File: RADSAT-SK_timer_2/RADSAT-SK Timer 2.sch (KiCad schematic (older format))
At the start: 54 parts, among them J201 Conn_01x07, J202 Conn_01x05, J203 Conn_01x03, J204 Conn_01x02, J205 Conn_01x02, J206 Conn_01x02, Q201 IRLML2060, Q202 IRLML2060, Q204 IRLML2060, Q205 IRLML2060, Q206 IRLML2060, Q207 IRLML2060, SW201 SW_Push, SW202 SW_Push, SW203 SW_Push, SW204 SW_Push, SW205 SW_Push, SW206 SW_Push, U202 LTC3440EMSPBF, U230 CPC1114N, U240 CPC1114N, U250 CPC1114N, U260 CPC1114N

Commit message: changed RBF logic and added footprint for J202
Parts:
- removed C204: 10uF, Capacitor_SMD:C_0805_2012Metric, symbol Device:C
- removed C205: 0.1uF, Capacitor_SMD:C_0805_2012Metric, symbol Device:C
- removed C207: 1.5nF, Capacitor_SMD:C_0805_2012Metric, symbol Device:C
- removed C208: 22uF, Capacitor_SMD:C_1210_3225Metric_Pad1.33x2.70mm_HandSolder, symbol Device:C
- removed D201: 5.0SMDJ5.0A, Diode_SMD:D_SMC_Handsoldering, symbol Diode:SM6T6V8A
- removed D203: MBRM120LT3G, Diode_SMD:D_Powermite_AK, symbol Device:D_Schottky
- removed J202: Conn_01x05, Connector_Hirose:Hirose_DF13-05P-1.25DSA_1x05_P1.25mm_Vertical, symbol Connector_Generic:Conn_01x05
- removed L201: 10uH, Sumida_inductor:Sumida_inductor, symbol Device:L
- removed Q201, Q202, Q207: IRLML2060, Package_TO_SOT_SMD:SOT-23_Handsoldering, symbol Transistor_FET:IRLML2060
- removed R201: 3M, Resistor_SMD:R_0805_2012Metric, symbol Device:R
- removed R202, R204, R220: 100, Resistor_SMD:R_0805_2012Metric, symbol Device:R
- removed R203, R221: 1M, Resistor_SMD:R_0805_2012Metric, symbol Device:R
- removed R205: 60.4K, Resistor_SMD:R_0805_2012Metric, symbol Device:R
- removed R206: 15k, Resistor_SMD:R_0805_2012Metric, symbol Device:R
- removed R207: 619k, Resistor_SMD:R_0805_2012Metric, symbol Device:R
- removed R208: 200k, Resistor_SMD:R_0805_2012Metric, symbol Device:R
- removed U202: LTC3440EMSPBF, Package_SO:MSOP-10_3x3mm_P0.5mm, symbol LTC3440EMSPBF:LTC3440EMSPBF
- added H101, H102, H103, H104: MountingHole, MountingHole:MountingHole_3.2mm_M3_ISO7380_Pad_TopBottom, symbol Mechanical:MountingHole
- added J101, J103: Conn_02x26_Odd_Even, Connector_PinSocket_2.54mm:PinSocket_2x26_P2.54mm_Vertical, symbol Connector_Generic:Conn_02x26_Odd_Even
- added J202: Conn_01x04_Female, Connector_Hirose:Hirose_DF13-04P-1.25DSA_1x04_P1.25mm_Vertical, symbol Connector:Conn_01x04_Female
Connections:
- wire segments 154 -> 103
- no-connect marks 3 -> 95
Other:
- note added: "CSKB Connectors"
- note added: "Mechanical Switches and RBF Connection with 5vCharge"
- note added: "Mounting Holes\n"
- note added: "RBF IN: Short Pins 4, 2\nRBF OUT: Pins OPEN\nCHARGE PIN: PINS 1,3 OPEN, 5V Pin 1"
- note added: "Riley Nemetz\nAtharva Kulkarni"
- note removed: "Battery Boost, Mechanical Switches and RBF Connection with 5vCharge"
- note removed: "RBF IN: Short Pins 1, 2\nRBF OUT: Pins OPEN\nCHARGE PIN: PINS 1,2 OPEN, 5V Pin 3"
- note removed: "Riley Nemetz"
- moved on the sheet: D204A, D204B, D206, J203, R209, R210, U230

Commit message: new RBF logic and charging circuit!!
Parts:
- removed J202: Conn_01x04_Female, Connector_Hirose:Hirose_DF13-04P-1.25DSA_1x04_P1.25mm_Vertical, symbol Connector:Conn_01x04_Female
- added BT202: Battery_Cell, Battery:BatteryHolder_Keystone_1060_1x2032, symbol Device:Battery_Cell
- added C?: 2.2uF, Capacitor_SMD:C_0805_2012Metric, symbol Device:C
- added C?: 7pF, Capacitor_SMD:C_0805_2012Metric, symbol Device:C
- added C?: 1uF, Capacitor_SMD:C_0805_2012Metric, symbol Device:C
- added C?: 0.1uF, Capacitor_SMD:C_0805_2012Metric, symbol Device:C
- added D?: RB751V40T1G, Diode_SMD:D_SOD-323, symbol Device:D_Schottky
- added D?: LED, LED_SMD:LED_0805_2012Metric, symbol Device:LED
- added J202: Conn_01x05_Female, symbol Connector:Conn_01x05_Female
- added R?: 560, Resistor_SMD:R_0805_2012Metric, symbol Device:R
- added R?: 1k, Resistor_SMD:R_0805_2012Metric, symbol Device:R
- added R?: 51.1k, Resistor_SMD:R_0805_2012Metric, symbol Device:R
- added R?: 76.8k, Resistor_SMD:R_0805_2012Metric, symbol Device:R
- added R?: 10k, Resistor_SMD:R_0805_2012Metric, symbol Device:R
- added R?: 100k, Resistor_SMD:R_0805_2012Metric, symbol Device:R
- added R?: 49.9k, Resistor_SMD:R_0805_2012Metric, symbol Device:R
- added R?: 604K, Resistor_SMD:R_0805_2012Metric, symbol Device:R
- added U201: LP2980IM5-5.0, Package_TO_SOT_SMD:TSOT-23-5, symbol RADSAT-SK-Timer-rescue:LP2980IM5-5.0-LP2980IM5-5.0
- added U202: TPS3700DDCR, Package_TO_SOT_SMD:TSOT-23-6, symbol RADSAT-SK-Timer-rescue:TPS3700DDCR-TPS3700DDCR
- renumbered BT202 to BT203, J101 to J201, J103 to J203
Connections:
- net labels added: A, B, CHRG_ON-OFF
- wire segments 103 -> 158
- no-connect marks 95 -> 96
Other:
- note added: "Battery Charging\n"
- moved on the sheet: D204A, D204B, D?, J201, J203, R209, R210, U230

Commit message: annotated part numbers (generated netlist)
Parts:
- gave numbers to parts that had none: 14
- renumbered D206 to D101, D205 to D104, H103 to H102, H102 to H103, J201 to J207, J203 to J208, Q206 to Q101, Q204 to Q102, Q205 to Q103, R217 to R109

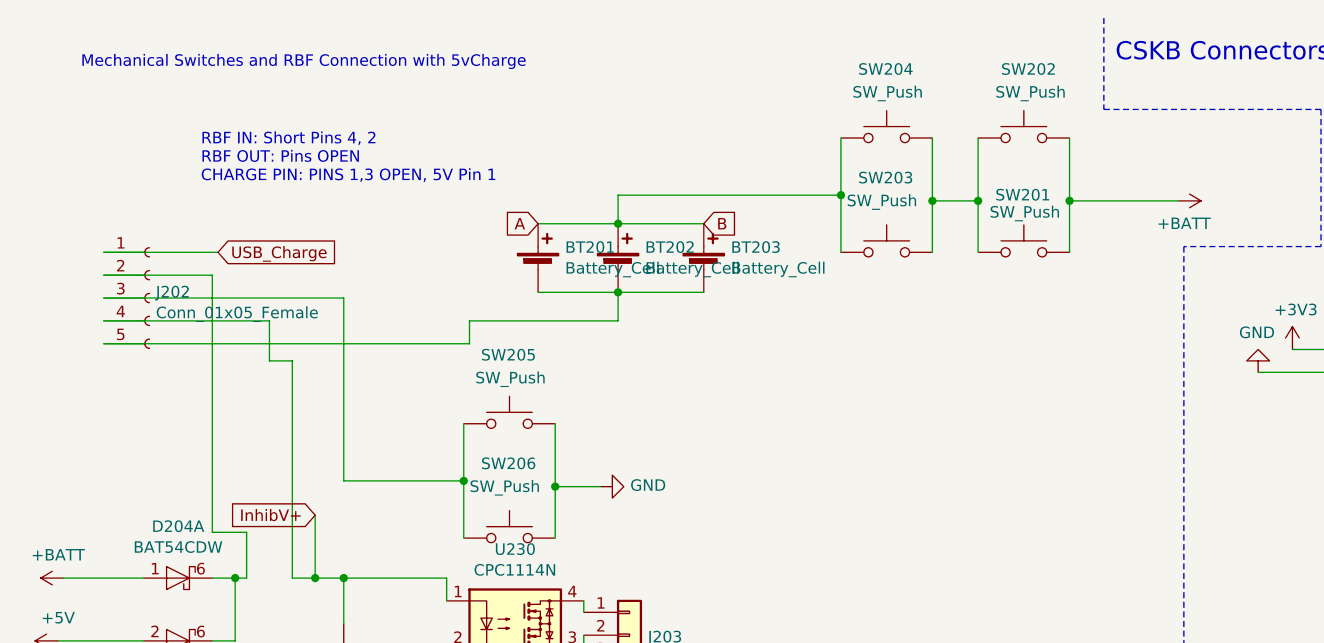
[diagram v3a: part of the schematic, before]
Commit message: switched out pin 3 and 5 on RBF pin
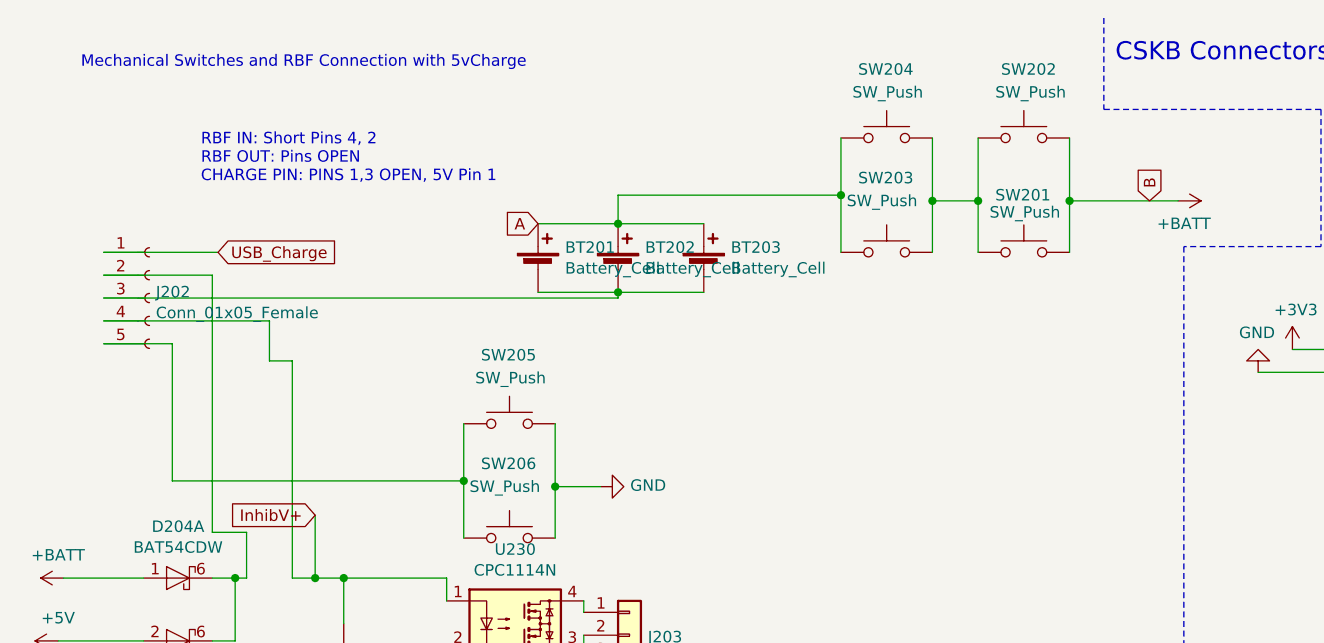
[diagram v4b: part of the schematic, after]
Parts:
- J202: footprint (none) -> Connector_Hirose:Hirose_DF13-05P-1.25DSA_1x05_P1.25mm_Vertical
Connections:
- wire segments 158 -> 156
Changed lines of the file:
@@
 Inhib_in
-$Comp
-L Device:Battery_Cell BT203
-U 1 1 600CC811
-P 3425 1575
-F 0 "BT203" H 3543 1671 50  0000 L CNN
-F 1 "Battery_Cell" H 3543 1580 50  0000 L CNN
-F 2 "Battery:BatteryHolder_Keystone_1060_1x2032" V 3425 1635 50  0001 C CNN
-F 3 "~" V 3425 1635 50  0001 C CNN
-	1    3425 1575
-	1    0    0    -1
-$EndComp
 $Comp
 L Device:Battery_Cell BT201
@@
 Wire Wire Line
 	2700 1675 3050 1675
-Wire Wire Line
-	3050 1800 3050 1675
 Connection ~ 3050 1675
 Wire Wire Line
@@
 Mounting Holes\n
 Wire Wire Line
-	2400 1900 2400 1800
-Wire Wire Line
-	2400 1800 3050 1800
-Wire Wire Line
-	800  1900 2400 1900
-Wire Wire Line
 	800  1800 1525 1800
 Wire Wire Line
@@
 Wire Wire Line
 	800  1500 1300 1500
-Wire Wire Line
-	800  1700 1850 1700
-Wire Wire Line
-	1850 1700 1850 2500
-Wire Wire Line
-	1850 2500 2375 2500
 $Comp
 L Connector:Conn_01x05_Female J202
@@
 F 0 "J202" H 1028 1726 50  0000 L CNN
 F 1 "Conn_01x05_Female" H 1028 1635 50  0000 L CNN
-F 2 "" H 1000 1700 50  0001 C CNN
+F 2 "Connector_Hirose:Hirose_DF13-05P-1.25DSA_1x05_P1.25mm_Vertical" H 1000 1700 50  0001 C CNN
 F 3 "~" H 1000 1700 50  0001 C CNN
 	1    1000 1700
@@
 Text GLabel 2700 1375 0    50   Input ~ 0
 A
-Text GLabel 3425 1375 2    50   Input ~ 0
-B
 Wire Wire Line
 	1625 2925 1725 2925
@@
 Text Notes 5375 5125 0    50   ~ 0
 Battery Charging\n
+$Comp
+L Device:Battery_Cell BT203
+U 1 1 600CC811
+P 3425 1575
+F 0 "BT203" H 3543 1671 50  0000 L CNN
+F 1 "Battery_Cell" H 3543 1580 50  0000 L CNN
+F 2 "Battery:BatteryHolder_Keystone_1060_1x2032" V 3425 1635 50  0001 C CNN
+F 3 "~" V 3425 1635 50  0001 C CNN
+	1    3425 1575
+	1    0    0    -1
+$EndComp
+Text GLabel 5375 1275 1    50   Input ~ 0
+B
+Wire Wire Line
+	1100 2500 1100 1900
+Wire Wire Line
+	1100 1900 800  1900
+Wire Wire Line
+	1100 2500 2375 2500
+Wire Wire Line
+	3050 1675 3050 1700
+Wire Wire Line
+	800  1700 3050 1700
 $EndSCHEMATC

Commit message: fixed RBF logic (back to initial state) and added test points
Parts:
- removed D101, D104: LED, LED_SMD:LED_0603_1608Metric_Pad1.05x0.95mm_HandSolder, symbol Device:LED
- removed R109, R209: 1k, Resistor_SMD:R_0805_2012Metric, symbol Device:R
- added J209: Conn_01x15, symbol Connector_Generic:Conn_01x15
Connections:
- net labels added: Test_CHRG_ON-OFF, Test_CSKB_3V3, Test_CSKB_5V, Test_GND, Test_I2C_CLK, Test_I2C_DATA, Test_INA+, Test_INB-, Test_InhibV+, Test_Relay_Inhibs, Test_SW1, Test_SW2, Test_USB_Charge, Test_Vreg, Test_negetive_Batt
- wire segments 156 -> 184

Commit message: deleted extra LEDs
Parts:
- removed D103: LED, LED_SMD:LED_0805_2012Metric, symbol Device:LED
- removed R106: 1k, Resistor_SMD:R_0805_2012Metric, symbol Device:R
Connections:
- wire segments 184 -> 180
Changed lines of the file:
@@
 Wire Wire Line
 	5450 4375 5525 4375
-Connection ~ 4975 4375
 $Comp
 L Device:D_Schottky D?
@@
 Wire Wire Line
 	4000 4700 3575 4700
-Connection ~ 4500 5050
-Wire Wire Line
-	4975 5050 4500 5050
-Wire Wire Line
-	4975 5025 4975 5050
 Connection ~ 4500 4375
-Wire Wire Line
-	4500 4375 4975 4375
-Wire Wire Line
-	4975 4675 4975 4725
-$Comp
-L Device:LED D?
-U 1 1 62C79500
-P 4975 4525
-AR Path="/62B9869E/62C79500" Ref="D?"  Part="1"
-AR Path="/62C79500" Ref="D103"  Part="1"
-F 0 "D103" V 5014 4407 50  0000 R CNN
-F 1 "LED" V 4923 4407 50  0000 R CNN
-F 2 "LED_SMD:LED_0805_2012Metric" H 4975 4525 50  0001 C CNN
-F 3 "~" H 4975 4525 50  0001 C CNN
-	1    4975 4525
-	0    -1   -1   0
-$EndComp
 Wire Wire Line
 	4000 5050 4275 5050
@@
 	1    5675 4375
 	0    -1   -1   0
-$EndComp
-$Comp
-L Device:R R?
-U 1 1 62C79529
-P 4975 4875
-AR Path="/62B9869E/62C79529" Ref="R?"  Part="1"
-AR Path="/62C79529" Ref="R106"  Part="1"
-F 0 "R106" H 5045 4921 50  0000 L CNN
-F 1 "1k" H 5045 4830 50  0000 L CNN
-F 2 "Resistor_SMD:R_0805_2012Metric" V 4905 4875 50  0001 C CNN
-F 3 "~" H 4975 4875 50  0001 C CNN
-	1    4975 4875
-	1    0    0    -1
 $EndComp
 $Comp
@@
 Wire Wire Line
 	5025 4150 5050 4150
-Wire Wire Line
-	4975 4375 5025 4375
 Connection ~ 5025 4375
 Wire Wire Line
@@
 Wire Wire Line
 	9025 4600 9200 4600
+Wire Wire Line
+	4500 4375 5025 4375
 $EndSCHEMATC

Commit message: added pull down resistors on relays
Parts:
- added R106, R109: 1M, symbol Device:R
- J209: footprint (none) -> Connector_Hirose:Hirose_DF13-15P-1.25DSA_1x15_P1.25mm_Vertical
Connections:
- wire segments 180 -> 185
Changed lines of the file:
@@
 	3100 6675 3100 7550
 Connection ~ 4475 7550
-Wire Wire Line
-	3100 6675 3025 6675
 Connection ~ 3100 6675
 Connection ~ 2925 6675
@@
 	2375 2525 2375 2750
 Wire Wire Line
-	2025 2925 2025 3275
-Wire Wire Line
-	1725 2925 2025 2925
+	2025 2925 2025 3525
+Wire Wire Line
+	1725 2925 1850 2925
 Connection ~ 2025 2925
 Wire Wire Line
@@
 Wire Notes Line
 	7950 5425 11225 5425
-Wire Wire Line
-	3025 6675 3025 7225
-Connection ~ 3025 6675
-Wire Wire Line
-	3025 6675 2925 6675
 Wire Wire Line
 	4525 1275 4525 850
@@
 F 0 "J209" V 10900 4525 50  0000 L CNN
 F 1 "Conn_01x15" V 10975 4400 50  0000 L CNN
-F 2 "" H 10800 4450 50  0001 C CNN
+F 2 "Connector_Hirose:Hirose_DF13-15P-1.25DSA_1x15_P1.25mm_Vertical" H 10800 4450 50  0001 C CNN
 F 3 "~" H 10800 4450 50  0001 C CNN
 	1    10800 4450
@@
 Text GLabel 10600 4050 0    50   Input ~ 0
 Test_SW2
-Text GLabel 2025 3275 3    50   Input ~ 0
+Text GLabel 2025 3525 3    50   Input ~ 0
 Test_InhibV+
 Text GLabel 10600 4150 0    50   Input ~ 0
@@
 Text GLabel 10600 4850 0    50   Input ~ 0
 Test_INB-
-Text GLabel 3025 7225 0    50   Input ~ 0
-Test_Relay_Inhibs
 Text GLabel 10600 4950 0    50   Input ~ 0
 Test_Relay_Inhibs
@@
 Wire Wire Line
 	4500 4375 5025 4375
+$Comp
+L Device:R R106
+U 1 1 62B16433
+P 2975 6950
+F 0 "R106" V 2875 6850 50  0000 L CNN
+F 1 "1M" V 2800 6900 50  0000 L CNN
+F 2 "" V 2905 6950 50  0001 C CNN
+F 3 "~" H 2975 6950 50  0001 C CNN
+	1    2975 6950
+	1    0    0    -1
+$EndComp
+$Comp
+L power:GND #PWR0122
+U 1 1 62B33151
+P 2975 7100
+F 0 "#PWR0122" H 2975 6850 50  0001 C CNN
+F 1 "GND" H 2875 7000 50  0000 C CNN
+F 2 "" H 2975 7100 50  0001 C CNN
+F 3 "" H 2975 7100 50  0001 C CNN
+	1    2975 7100
+	1    0    0    -1
+$EndComp
+Wire Wire Line
+	2975 6675 2975 6800
+Connection ~ 2975 6675
+Wire Wire Line
+	2975 6675 2925 6675
+Text GLabel 3000 7425 0    50   Input ~ 0
+Test_Relay_Inhibs
+Wire Wire Line
+	3050 6675 2975 6675
+Connection ~ 3050 6675
+Wire Wire Line
+	3100 6675 3050 6675
+Wire Wire Line
+	3050 7425 3000 7425
+Wire Wire Line
+	3050 6675 3050 7425
+Wire Wire Line
+	1850 2925 1850 3250
+Connection ~ 1850 2925
+Wire Wire Line
+	1850 2925 2025 2925
+$Comp
+L Device:R R109
+U 1 1 62BC56F8
+P 1850 3400
+F 0 "R109" V 1750 3300 50  0000 L CNN
+F 1 "1M" V 1675 3350 50  0000 L CNN
+F 2 "" V 1780 3400 50  0001 C CNN
+F 3 "~" H 1850 3400 50  0001 C CNN
+	1    1850 3400
+	1    0    0    -1
+$EndComp
+$Comp
+L power:GND #PWR0123
+U 1 1 62BC77F7
+P 1850 3550
+F 0 "#PWR0123" H 1850 3300 50  0001 C CNN
+F 1 "GND" H 1855 3377 50  0000 C CNN
+F 2 "" H 1850 3550 50  0001 C CNN
+F 3 "" H 1850 3550 50  0001 C CNN
+	1    1850 3550
+	1    0    0    -1
+$EndComp
 $EndSCHEMATC

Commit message: added resistors in schematic, changed Voltage regulator
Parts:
- removed C104: 7pF, Capacitor_SMD:C_0805_2012Metric, symbol Device:C
- removed U201: LP2980IM5-5.0, Package_TO_SOT_SMD:TSOT-23-5, symbol RADSAT-SK-Timer-rescue:LP2980IM5-5.0-LP2980IM5-5.0
- added R110: 60, Resistor_SMD:R_0805_2012Metric, symbol Device:R
- added R111: 17, Resistor_SMD:R_0805_2012Metric, symbol Device:R
- added U101: LT1521IS8-5TR, LT1521IS8-5TR:SO-8_S, symbol LT1521IS8-5TR:LT1521IS8-5TR
- C103: value 2.2uF -> C
- R103: value 560 -> R
- R104: value 76.8k -> R
- R106, R109: footprint (none) -> Resistor_SMD:R_0805_2012Metric
- R107: value 51.1k -> 81
- R210: value 1k -> 320
- R211, R213, R215: value 100 -> 25
- R212, R214, R216: value 1k -> 80
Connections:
- no-connect marks 96 -> 95
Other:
- moved on the sheet: C102, D102, J201
